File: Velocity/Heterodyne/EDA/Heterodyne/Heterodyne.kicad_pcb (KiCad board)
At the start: 2 copper layers, 15 parts, among them J1 Doppler Out, J2 V_Square, J3 Conn_01x02, U1 SA612AD

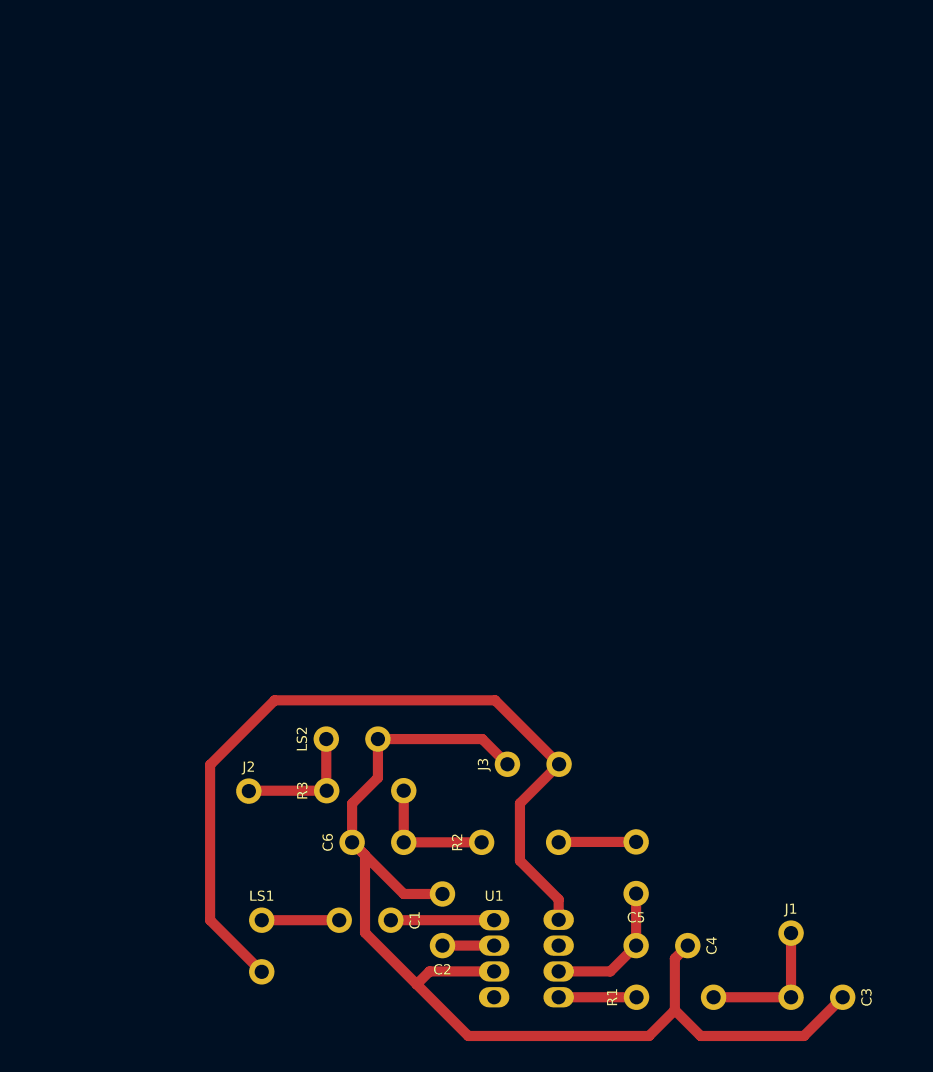
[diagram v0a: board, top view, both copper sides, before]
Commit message: added oscilator for heterodyne circuit
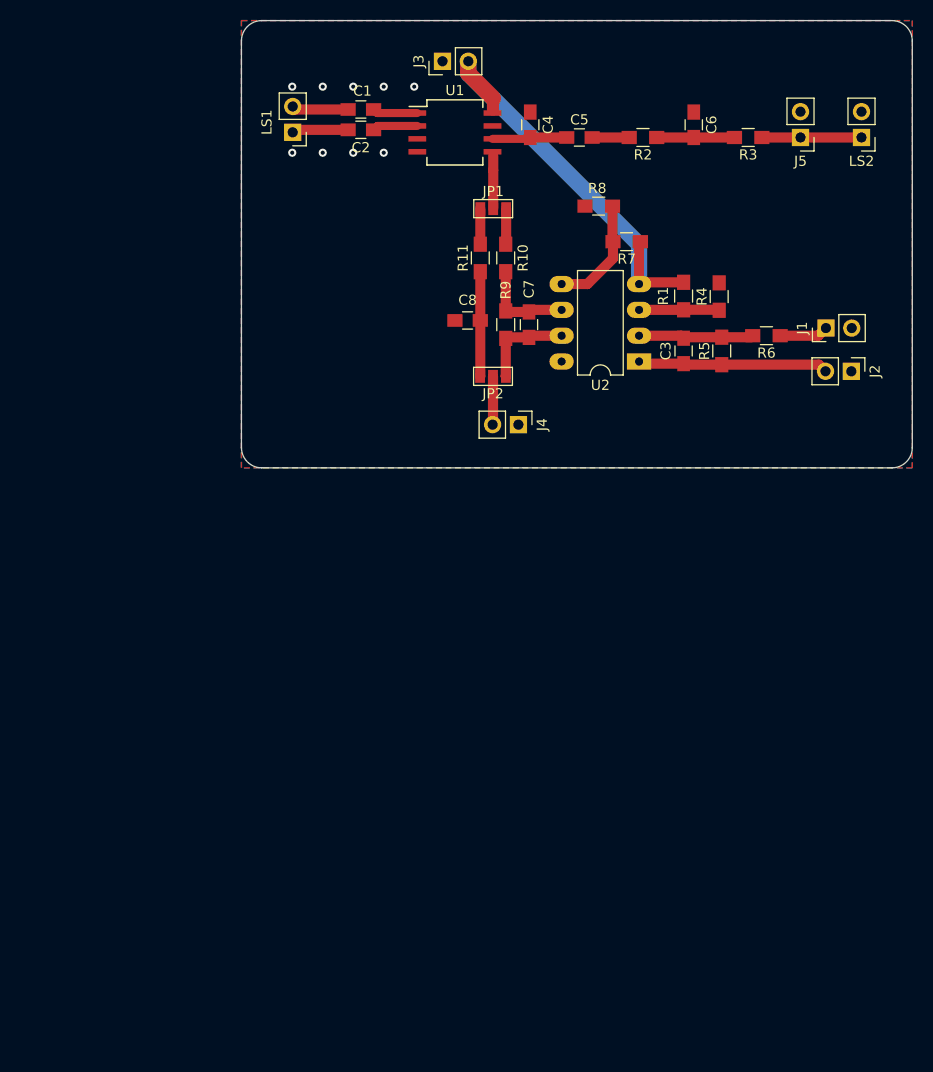
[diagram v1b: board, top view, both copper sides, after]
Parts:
- added C7: 680 pF, Capacitors_SMD:C_0805_HandSoldering, F.Cu at (153.3, 65.9)
- added C8: 680 pF, Capacitors_SMD:C_0805_HandSoldering, F.Cu at (147.2, 65.5)
- added J4: Doppler_Out, Pin_Headers:Pin_Header_Straight_1x02_Pitch2.54mm, F.Cu at (152.2, 75.8)
- added J5: V_Square, Pin_Headers:Pin_Header_Straight_1x02_Pitch2.54mm, F.Cu at (180.0, 47.5)
- added JP1: Jumper_NC_Dual, Connectors:GS3, F.Cu at (149.8, 54.5)
- added JP2: Jumper_NC_Dual, Connectors:GS3, F.Cu at (149.8, 71.0)
- added R10: 1 kΩ, Resistors_SMD:R_0805_HandSoldering, F.Cu at (151.0, 59.4)
- added R11: 2.2 kΩ, Resistors_SMD:R_0805_HandSoldering, F.Cu at (148.5, 59.4)
- added R4: 3.3 kΩ, Resistors_SMD:R_0805_HandSoldering, F.Cu at (172.0, 63.1)
- added R5: 2.2 kΩ, Resistors_SMD:R_0805_HandSoldering, F.Cu at (172.2, 68.5)
- added R6: 1 kΩ, Resistors_SMD:R_0805_HandSoldering, F.Cu at (176.7, 67.0)
- added R7: 3.3 kΩ, Resistors_SMD:R_0805_HandSoldering, F.Cu at (162.9, 57.8)
- added R8: 3.3 kΩ, Resistors_SMD:R_0805_HandSoldering, F.Cu at (160.2, 54.2)
- added R9: 2.2 kΩ, Resistors_SMD:R_0805_HandSoldering, F.Cu at (151.0, 65.9)
- added U2: NE5532, Housings_DIP:DIP-8_W7.62mm_LongPads, F.Cu at (164.1, 69.5)
- C1, C2, C4, C5, C6: footprint Turbitidy:Voltera_Conn_01x02 -> Capacitors_SMD:C_0805_HandSoldering
- C3: value 33 nF -> 680 pF; footprint Turbitidy:Voltera_Conn_01x02 -> Capacitors_SMD:C_0805_HandSoldering
- J1: value Doppler Out -> OP_IN; footprint Turbitidy:Voltera_Conn_01x01 -> Pin_Headers:Pin_Header_Straight_1x02_Pitch2.54mm
- J2: value V_Square -> OP_OUT; footprint Turbitidy:Voltera_Conn_01x01 -> Pin_Headers:Pin_Header_Straight_1x02_Pitch2.54mm
- J3: value Conn_01x02 -> PWR; footprint Turbitidy:Voltera_Conn_01x02 -> Pin_Headers:Pin_Header_Straight_1x02_Pitch2.54mm
- LS1: value Emmiter -> Receiver; footprint Turbitidy:Voltera_Conn_01x02 -> Pin_Headers:Pin_Header_Straight_1x02_Pitch2.54mm
- LS2: footprint Turbitidy:Voltera_Conn_01x02 -> Pin_Headers:Pin_Header_Straight_1x02_Pitch2.54mm
- R1: value 330 Ω -> 3.3 kΩ; footprint Turbitidy:Voltera_Conn_01x02_Space -> Resistors_SMD:R_0805_HandSoldering
- R2, R3: footprint Turbitidy:Voltera_Conn_01x02_Space -> Resistors_SMD:R_0805_HandSoldering
- U1: footprint Turbitidy:Voltera_DIP8 -> Housings_SOIC:SO-8_5.3x6.2mm_Pitch1.27mm
- moved C4 82.2 mm to (153.4, 46.2)
- moved C2 80.7 mm to (136.8, 46.7)
- moved C1 79.8 mm to (136.8, 44.7), turned to 180 degrees
- moved LS2 79.2 mm to (186.0, 47.5), turned to 180 degrees
- moved C6 78.2 mm to (169.5, 46.2), turned to 270 degrees
- moved U1 77.6 mm to (146.0, 47.0)
- moved LS1 77.5 mm to (130.0, 47.0), turned to 180 degrees
- moved R3 76.5 mm to (174.8, 47.5), turned to 180 degrees
- moved C5 74.6 mm to (158.2, 47.5), turned to 0 degrees
- moved J2 72.2 mm to (185.0, 70.5), turned to 270 degrees
- moved R2 71.1 mm to (164.5, 47.5), turned to 180 degrees
- moved J3 69.5 mm to (144.8, 40.0)
- moved R1 69.1 mm to (168.5, 63.1), turned to 270 degrees
- moved C3 65.5 mm to (168.5, 68.5), turned to 90 degrees
- moved J1 59.6 mm to (182.5, 66.2), turned to 90 degrees
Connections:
- C2 pad 2: GND -> Net-(C2-Pad2)
- C3 pad 1: GND -> Net-(C3-Pad1)
- J1 pad 1: Net-(C3-Pad2) -> Net-(J1-Pad1)
- J2 pad 1: Net-(J2-Pad1) -> GND
- LS1 pad 1: Net-(C1-Pad2) -> Net-(C2-Pad2)
- LS1 pad 2: VPP -> Net-(C1-Pad2)
- LS2 pad 1: Net-(J2-Pad1) -> Net-(J5-Pad1)
- R1 pad 1: Net-(R1-Pad1) -> VPP
- R1 pad 2: Net-(C3-Pad2) -> Net-(R1-Pad2)
- R3 pad 1: Net-(J2-Pad1) -> Net-(J5-Pad1)
- U1 pad 5: Net-(R1-Pad1) -> Net-(JP1-Pad2)
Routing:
- net GND: track 115.3 -> 0.00 mm, vias 0 -> 9
- net VPP: track 80.5 -> 43.3 mm
- net Net-(C3-Pad1): track 0.00 -> 18.7 mm
- net Net-(J2-Pad1): track 12.8 -> 0.00 mm
- net Net-(R7-Pad2): track 0.00 -> 11.3 mm
- net Net-(C8-Pad1): track 0.00 -> 10.3 mm
- net Net-(J5-Pad1): track 0.00 -> 9.80 mm
- net Net-(C7-Pad2): track 0.00 -> 9.49 mm
- net Net-(C7-Pad1): track 0.00 -> 9.38 mm
- net Net-(R1-Pad2): track 0.00 -> 7.90 mm
- net Net-(R1-Pad1): track 7.66 -> 0.00 mm
- net Net-(C4-Pad2): track 13.8 -> 7.36 mm
- net Net-(C1-Pad1): track 10.2 -> 4.44 mm
- net Net-(C2-Pad2): track 0.00 -> 5.55 mm
- net Net-(JP1-Pad2): track 0.00 -> 5.23 mm
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- added copper zone on B.Cu, net GND
- added copper zone on F.Cu, net GND
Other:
- board outline added: 66 x 44 mm

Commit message: added bom and pcb files for velocity sensor
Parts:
- added C10: 330 pF, Capacitors_SMD:C_0805_HandSoldering, F.Cu at (156.2, 50.9)
- added C11: 330 μF, Capacitors_SMD:CP_Elec_8x10, F.Cu at (155.2, 42.4)
- added C12: 330 pF, Capacitors_SMD:C_0805_HandSoldering, F.Cu at (163.8, 50.8)
- added C13: 1 μF, Capacitors_SMD:C_1206_HandSoldering, F.Cu at (173.6, 45.0)
- added C14: 1 μF, Capacitors_SMD:C_1206_HandSoldering, F.Cu at (157.8, 61.0)
- added C9: 330 pF, Capacitors_SMD:C_0805_HandSoldering, F.Cu at (152.6, 49.5)
- added J6: OP_OUT, Pin_Headers:Pin_Header_Straight_1x02_Pitch2.54mm, F.Cu at (162.3, 77.8)
- added J7: Reciever, Pin_Headers:Pin_Header_Straight_1x01_Pitch2.54mm, F.Cu at (177.8, 55.8)
- added J8: Emmiter, Pin_Headers:Pin_Header_Straight_1x01_Pitch2.54mm, F.Cu at (129.8, 42.8)
- added U3: MAX7375AXR105, TO_SOT_Packages_SMD:SOT-323_SC-70_Handsoldering, F.Cu at (173.0, 48.6)
- C3, C7, C8: value 680 pF -> 100 nF
- C4, C5: value 1 nF -> 100 nF
- C6: value 2.2 nF -> 100 nF
- R1, R4, R7, R8: value 3.3 kΩ -> 10 kΩ
- R11: value 2.2 kΩ -> 330 Ω
- R2: value 680 Ω -> 3.3 kΩ
- R3: value 20 Ω -> 10 kΩ
- R5: value 2.2 kΩ -> 10 kΩ
- R6: value 1 kΩ -> 10 kΩ
- R9: value 2.2 kΩ -> 40 kΩ
- moved C4 31.3 mm to (175.3, 68.7)
- moved R6 29.7 mm to (149.3, 55.5), turned to 270 degrees
- moved C5 25.7 mm to (164.7, 72.4), turned to 180 degrees
- moved C6 23.1 mm to (150.6, 59.4), turned to 0 degrees
- moved R8 21.4 mm to (142.3, 66.0), turned to 270 degrees
- moved R3 20.4 mm to (170.3, 67.4)
- moved J3 18.2 mm to (162.8, 42.8), turned to 0 degrees
- moved LS2 16.6 mm to (171.7, 55.8), turned to 90 degrees
- moved R7 14.6 mm to (149.3, 63.0), turned to 270 degrees
- moved R10 13.3 mm to (159.9, 49.5), turned to 180 degrees
- moved J2 13.1 mm to (174.2, 63.0)
- moved J1 12.7 mm to (177.2, 77.8)
- moved J5 9.57 mm to (171.7, 52.2), turned to 90 degrees
- moved R4 9.40 mm to (170.3, 72.4), turned to 180 degrees
- moved JP1 8.93 mm to (141.1, 56.5)
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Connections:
- C4 pad 1: GND -> Net-(C3-Pad1)
- C5 pad 2: Net-(C5-Pad2) -> Net-(C3-Pad2)
- C6 pad 1: GND -> Net-(C6-Pad1)
- J2 pad 2: Net-(C3-Pad1) -> Net-(J2-Pad2)
- JP1 pad 1: Net-(JP1-Pad1) -> Net-(C7-Pad2)
- JP2 pad 3: Net-(C7-Pad1) -> Net-(C6-Pad2)
- R1 pad 1: VPP -> Net-(C3-Pad1)
- R1 pad 2: Net-(R1-Pad2) -> Net-(C3-Pad2)
- R10 pad 1: Net-(JP1-Pad1) -> Net-(C12-Pad1)
- R10 pad 2: Net-(C7-Pad2) -> Net-(C10-Pad2)
- R2 pad 1: Net-(C6-Pad2) -> Net-(J5-Pad1)
- R2 pad 2: Net-(C5-Pad2) -> Net-(C12-Pad1)
- R3 pad 1: Net-(J5-Pad1) -> Net-(J2-Pad2)
- R3 pad 2: Net-(C6-Pad2) -> Net-(C3-Pad1)
- R4 pad 1: Net-(R1-Pad2) -> Net-(J1-Pad1)
- R4 pad 2: GND -> Net-(C4-Pad2)
- R5 pad 1: Net-(C3-Pad1) -> Net-(C4-Pad2)
- R6 pad 1: Net-(J1-Pad1) -> Net-(R6-Pad1)
- R6 pad 2: Net-(C3-Pad2) -> Net-(C6-Pad1)
- R7 pad 1: VPP -> Net-(C6-Pad1)
- R7 pad 2: Net-(R7-Pad2) -> Net-(C7-Pad1)
- R8 pad 1: Net-(R7-Pad2) -> Net-(C7-Pad2)
- R8 pad 2: GND -> Net-(R8-Pad2)
- R9 pad 1: Net-(C7-Pad1) -> Net-(R8-Pad2)
- R9 pad 2: Net-(C7-Pad2) -> Net-(C6-Pad2)
- U1 pad 4: (no net) -> Net-(JP1-Pad2)
- U1 pad 5: Net-(JP1-Pad2) -> Net-(R6-Pad1)
- U1 pad 6: Net-(C4-Pad2) -> Net-(C9-Pad2)
- U2 pad 1: Net-(C3-Pad1) -> Net-(C3-Pad2)
- U2 pad 2: Net-(C3-Pad2) -> Net-(C4-Pad2)
- U2 pad 3: Net-(R1-Pad2) -> Net-(C3-Pad1)
- U2 pad 5: Net-(R7-Pad2) -> Net-(C7-Pad1)
- U2 pad 6: Net-(C7-Pad2) -> Net-(R8-Pad2)
- U2 pad 7: Net-(C7-Pad1) -> Net-(C6-Pad2)
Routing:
- net Net-(C6-Pad2): track 7.65 -> 26.2 mm
- net Net-(C4-Pad2): track 7.36 -> 25.3 mm, vias 0 -> 1
- net Net-(R7-Pad2): track 11.3 -> 0.00 mm
- net Net-(R8-Pad2): track 0.00 -> 10.0 mm
- net VPP: track 43.3 -> 51.6 mm
- net Net-(R1-Pad2): track 7.90 -> 0.00 mm
- net Net-(C3-Pad2): track 11.5 -> 17.7 mm
- net Net-(C3-Pad1): track 18.7 -> 24.1 mm
- net Net-(C12-Pad1): track 0.00 -> 4.98 mm
- net Net-(C6-Pad1): track 0.00 -> 4.80 mm
- net Net-(C10-Pad2): track 0.00 -> 4.80 mm
- net Net-(J2-Pad2): track 0.00 -> 4.40 mm
- net Net-(C7-Pad1): track 9.38 -> 5.35 mm
- net Net-(C5-Pad2): track 3.65 -> 0.00 mm
- net Net-(R6-Pad1): track 0.00 -> 3.63 mm
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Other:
- board size 66 x 44 mm -> 59 x 44 mm

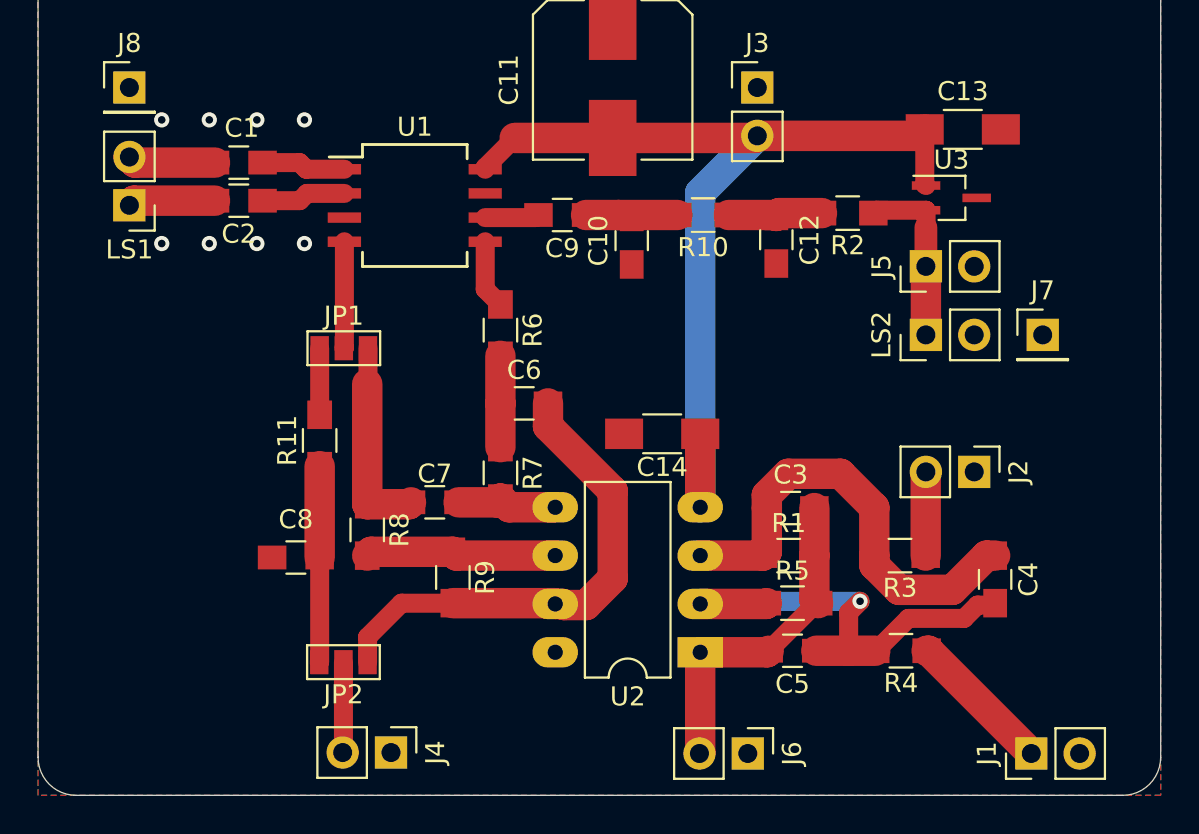
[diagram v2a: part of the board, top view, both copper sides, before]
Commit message: changed up velocity heterodyne schematic to fix issues with wireing, and so provide a channel for sine wave driver amplification
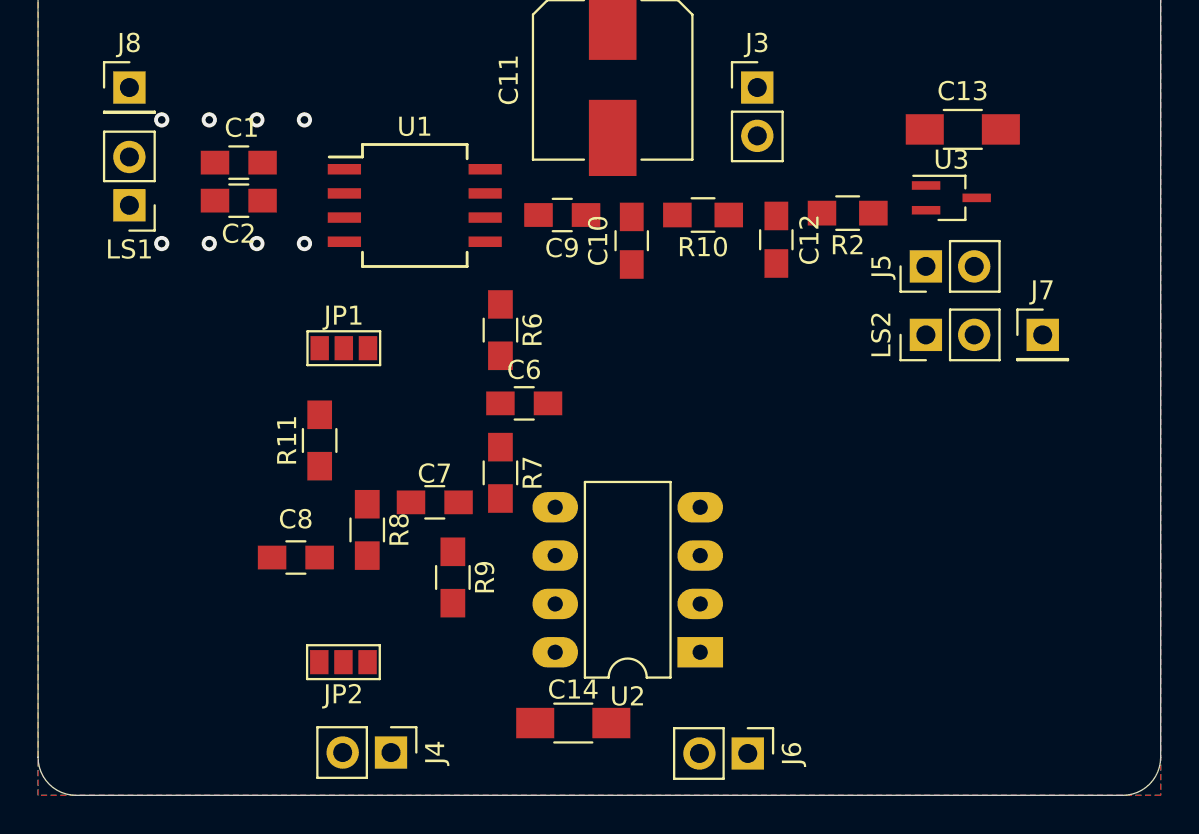
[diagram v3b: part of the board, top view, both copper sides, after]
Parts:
- removed C3, C4, C5: 100 nF, Capacitors_SMD:C_0805_HandSoldering
- removed J1: OP_IN, Pin_Headers:Pin_Header_Straight_1x02_Pitch2.54mm
- removed J2: OP_OUT, Pin_Headers:Pin_Header_Straight_1x02_Pitch2.54mm
- removed R1, R3, R4, R5: 10 kΩ, Resistors_SMD:R_0805_HandSoldering
- R9: value 40 kΩ -> 39 kΩ
- moved C14 15.9 mm to (153.1, 76.2), turned to 0 degrees
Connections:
- C10 pad 2: Net-(C10-Pad2) -> Driver_Wave
- C11 pad 1: GND -> VPP
- C11 pad 2: VPP -> GND
- C9 pad 1: Net-(C10-Pad2) -> Driver_Wave
- R10 pad 2: Net-(C10-Pad2) -> Driver_Wave
- U1 pad 7: (no net) -> Net-(U1-Pad7)
- U2 pad 3: Net-(C3-Pad1) -> Driver_Wave
- U2 pad 4: VPP -> GND
- U2 pad 8: GND -> VPP
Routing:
- net VPP: track 51.6 -> 0.00 mm
- net Net-(C6-Pad2): track 26.2 -> 0.00 mm
- net Net-(R1-Pad2): track 25.3 -> 0.00 mm, vias 1 -> 0
- net Net-(C3-Pad1): track 24.1 -> 0.00 mm
- net Net-(J6-Pad2): track 17.7 -> 0.00 mm
- net Net-(C7-Pad2): track 10.5 -> 0.00 mm
- net Net-(C8-Pad1): track 10.3 -> 0.00 mm
- net Net-(R8-Pad2): track 10.0 -> 0.00 mm
- net Net-(J5-Pad1): track 9.39 -> 0.00 mm
- net Net-(J1-Pad1): track 7.74 -> 0.00 mm
- net Net-(JP1-Pad2): track 5.61 -> 0.00 mm
- net Net-(C7-Pad1): track 5.35 -> 0.00 mm
- net Net-(C12-Pad1): track 4.98 -> 0.00 mm
- net Net-(C6-Pad1): track 4.80 -> 0.00 mm
- net Net-(C10-Pad2): track 4.80 -> 0.00 mm
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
